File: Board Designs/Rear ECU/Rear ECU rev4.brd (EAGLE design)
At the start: 87.8 x 143.2 mm, 97 parts, among them X1 CONNECTOR-2, X2 CONNECTOR-6, X3 CONNECTOR-10MX150L_VERTICAL-10, X4 CONNECTOR-10MX150L_VERTICAL-10

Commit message: Rear ECU rev4: remove reference to unconnected/unused GPIO_CTRL3
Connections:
- removed net GPIO_CTRL3: U$3.D13
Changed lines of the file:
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@@
 <wire x1="22.987" y1="46.609" x2="21.463" y2="45.085" width="0.4064" layer="16"/>
-</signal>
-<signal name="GPIO_CTRL3">
-<contactref element="U$3" pad="D13"/>
 </signal>
 <signal name="GPIO_CTRL1">

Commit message: Add 15-pin .1" header to library, update copper rubout instructions on Enerdel board, add cooling control mosfet part numbers to Rear ECU schematic, fix silkscreen fuse names in Front ECU rev6
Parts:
- U$2, U$4, U$5: value N-CHANNEL_MOSFETGENERIC -> TK8R2A06PL
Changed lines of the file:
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@@
 <element name="C3" library="HyTechDevices" package="0805" value="1uF" x="78.701" y="114.366" rot="R90"/>
 <element name="C4" library="HyTechDevices" package="0805" value="1uF" x="72.758" y="109.894"/>
-<element name="U$2" library="HyTechDevices" package="TO-220-SINK" value="N-CHANNEL_MOSFETGENERIC" x="74.758" y="42.792">
+<element name="U$2" library="HyTechDevices" package="TO-220-SINK" value="TK8R2A06PL" x="74.758" y="42.792">
 <attribute name="_EXTERNAL_" value="1" x="74.758" y="42.792" size="1.778" layer="27" display="off"/>
 </element>
-<element name="U$4" library="HyTechDevices" package="TO-220-SINK" value="N-CHANNEL_MOSFETGENERIC" x="74.758" y="27.094">
+<element name="U$4" library="HyTechDevices" package="TO-220-SINK" value="TK8R2A06PL" x="74.758" y="27.094">
 <attribute name="_EXTERNAL_" value="1" x="74.758" y="27.094" size="1.778" layer="27" display="off"/>
 </element>
-<element name="U$5" library="HyTechDevices" package="TO-220-SINK" value="N-CHANNEL_MOSFETGENERIC" x="74.758" y="10.126">
+<element name="U$5" library="HyTechDevices" package="TO-220-SINK" value="TK8R2A06PL" x="74.758" y="10.126">
 <attribute name="_EXTERNAL_" value="1" x="74.758" y="10.126" size="1.778" layer="27" display="off"/>
 </element>

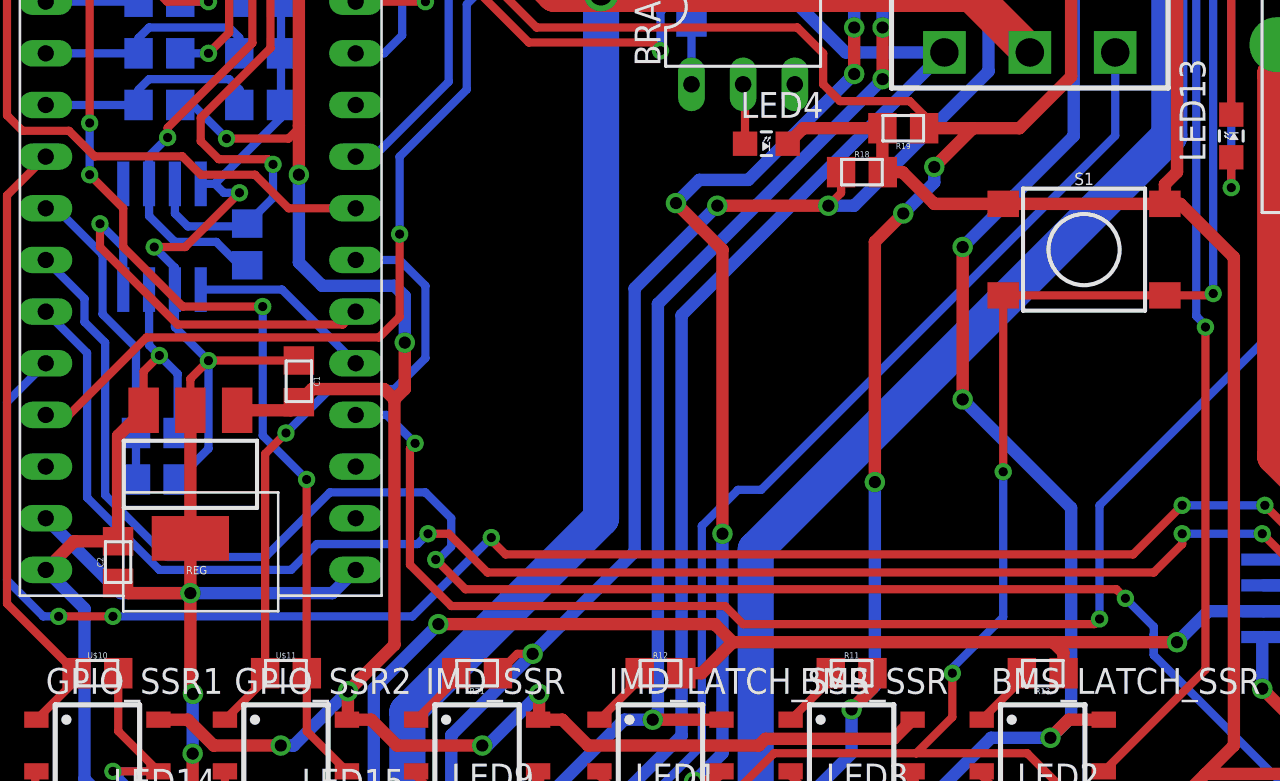
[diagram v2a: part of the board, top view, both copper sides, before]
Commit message: Added pulldown resistors to all gate drivers
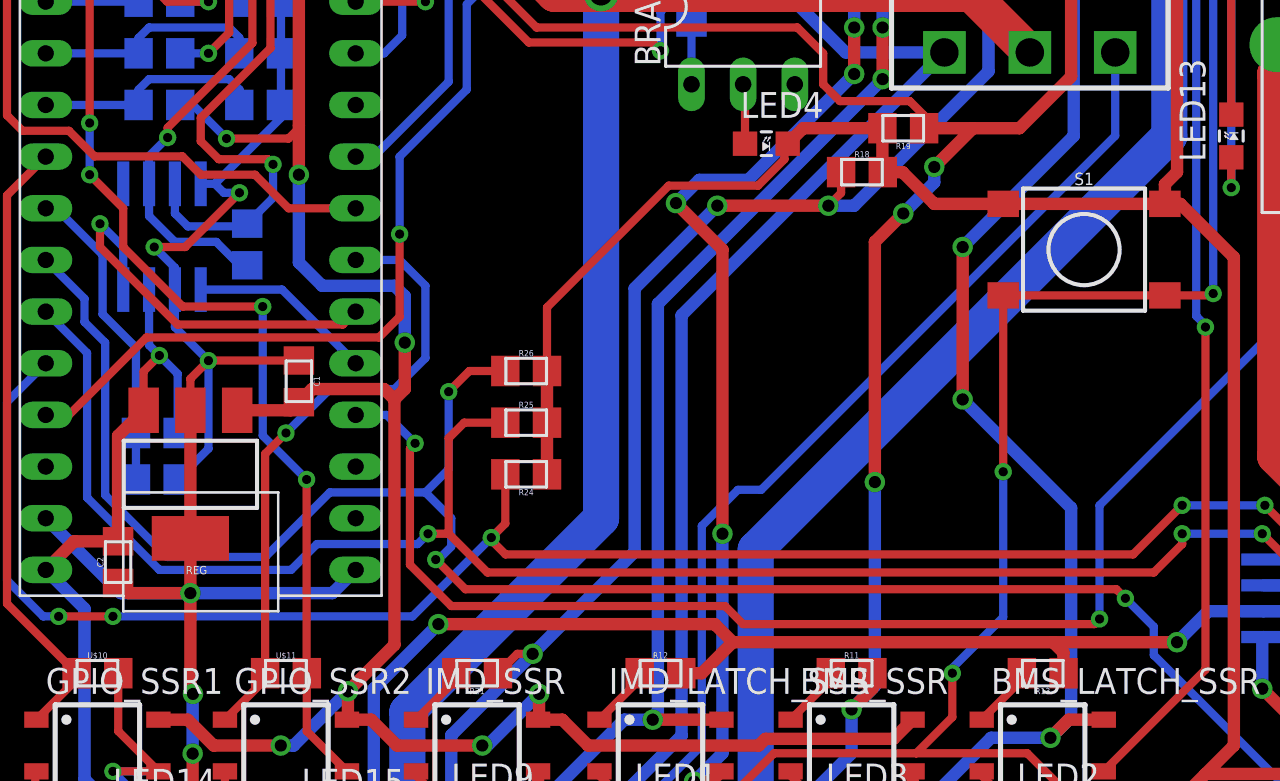
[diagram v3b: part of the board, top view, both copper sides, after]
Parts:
- added R24, R25, R26: 33, HyTechDevices:0805
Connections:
- net GND: now also R24.1, R25.2, R26.2
- net PWM_CTRL1: now also R24.2
- net PWM_CTRL2: now also R25.1
- net PWM_CTRL3: now also R26.1
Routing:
- net GND: track 522.5 -> 551.3 mm
- net PWM_CTRL2: track 80.3 -> 88.1 mm
- net PWM_CTRL3: track 102.9 -> 110.5 mm, vias 4 -> 5
- net PWM_CTRL1: track 85.2 -> 88.6 mm
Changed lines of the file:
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@@
 <?xml version="1.0" encoding="utf-8"?>
 <!DOCTYPE eagle SYSTEM "eagle.dtd">
-<eagle version="8.4.1">
+<eagle version="8.3.1">
 <drawing>
 <settings>
@@
 <param name="dpMaxLengthDifference" value="10mm"/>
 <param name="dpGapFactor" value="2.5"/>
+<param name="checkGrid" value="0"/>
 <param name="checkAngle" value="0"/>
 <param name="checkFont" value="1"/>
 <param name="checkRestrict" value="1"/>
-<param name="checkStop" value="0"/>
 <param name="useDiameter" value="13"/>
 <param name="maxErrors" value="50"/>
@@
 <element name="FSAE_FUSE" library="HyTechDevices" package="MINI-BLADE_FUSE_HOLDER" value="8A" x="24.384" y="138.43" rot="R180"/>
 <element name="SHUTDWN_FUSE" library="HyTechDevices" package="MINI-BLADE_FUSE_HOLDER" value="5A" x="7.112" y="78.232" rot="R90"/>
+<element name="R24" library="HyTechDevices" package="0805" value="33" x="27.94" y="40.894" rot="R180"/>
+<element name="R25" library="HyTechDevices" package="0805" value="33" x="27.94" y="43.434"/>
+<element name="R26" library="HyTechDevices" package="0805" value="33" x="27.94" y="45.974"/>
 </elements>
 <signals>
@@
 <wire x1="10.804" y1="40.64" x2="12.319" y2="42.155" width="0.4064" layer="16"/>
 <wire x1="12.319" y1="42.155" x2="12.319" y2="46.482" width="0.4064" layer="16"/>
-<wire x1="11.43" y1="44.044" x2="11.43" y2="37.744" width="0.6096" layer="1"/>
+<wire x1="11.43" y1="37.744" x2="11.43" y2="44.044" width="0.6096" layer="1"/>
 <via x="11.43" y="35.052" extent="1-16" drill="0.6"/>
-<wire x1="11.43" y1="37.744" x2="11.43" y2="35.052" width="0.6096" layer="1"/>
 <wire x1="7.874" y1="35.551" x2="8.373" y2="35.052" width="0.6096" layer="1"/>
-<wire x1="8.373" y1="35.052" x2="11.43" y2="35.052" width="0.6096" layer="1"/>
+<wire x1="11.43" y1="35.052" x2="8.373" y2="35.052" width="0.6096" layer="1"/>
 <wire x1="16.764" y1="104.405" x2="19.177" y2="106.818" width="0.6096" layer="16"/>
 <wire x1="19.177" y1="106.818" x2="19.177" y2="109.4994" width="0.6096" layer="16"/>
@@
 <wire x1="62.738" y1="51.562" x2="62.738" y2="27.559" width="0.6096" layer="1"/>
 <wire x1="62.738" y1="27.559" x2="61.341" y2="26.162" width="0.6096" layer="1"/>
-<wire x1="41.563" y1="57.912" x2="40.801" y2="57.15" width="0.6096" layer="1"/>
+<wire x1="40.801" y1="57.15" x2="41.563" y2="57.912" width="0.6096" layer="1"/>
 <wire x1="48.006" y1="54.193" x2="51.397" y2="54.193" width="0.6096" layer="1"/>
 <wire x1="19.558" y1="36.195" x2="18.415" y2="35.052" width="0.6096" layer="16"/>
@@
 <wire x1="33.81" y1="123.7528" x2="29.6912" y2="119.634" width="2.286" layer="16"/>
 <wire x1="29.6912" y1="119.634" x2="15.494" y2="119.634" width="2.286" layer="16"/>
+<contactref element="R24" pad="1"/>
+<contactref element="R25" pad="2"/>
+<contactref element="R26" pad="2"/>
+<wire x1="11.43" y1="37.744" x2="11.43" y2="35.052" width="0.6096" layer="1"/>
+<wire x1="28.965" y1="43.434" x2="28.965" y2="45.974" width="0.6096" layer="1"/>
+<wire x1="28.965" y1="43.434" x2="28.965" y2="40.894" width="0.6096" layer="1"/>
+<wire x1="28.965" y1="40.894" x2="28.965" y2="49.10253125" width="0.4064" layer="1"/>
+<wire x1="28.965" y1="49.10253125" x2="34.95026875" y2="55.0878" width="0.4064" layer="1"/>
+<wire x1="39.3398" y1="55.0878" x2="40.64" y2="56.388" width="0.4064" layer="1"/>
+<wire x1="34.95026875" y1="55.0878" x2="39.3398" y2="55.0878" width="0.4064" layer="1"/>
+<wire x1="40.64" y1="56.388" x2="40.64" y2="56.989" width="0.4064" layer="1"/>
+<wire x1="40.64" y1="56.989" x2="40.801" y2="57.15" width="0.4064" layer="1"/>
 </signal>
 <signal name="N$2">
@@
 <via x="57.404" y="34.798" extent="1-16" drill="0.45"/>
 <wire x1="57.404" y1="34.798" x2="58.801" y2="33.401" width="0.4064" layer="16"/>
-<wire x1="58.801" y1="33.02" x2="58.801" y2="33.401" width="0.4064" layer="16"/>
-<wire x1="58.801" y1="33.02" x2="58.801" y2="32.004" width="0.4064" layer="16"/>
 <wire x1="65.913" y1="24.892" x2="58.801" y2="32.004" width="0.4064" layer="16"/>
-<wire x1="58.801" y1="32.004" x2="58.801" y2="33.02" width="0.4064" layer="16"/>
+<wire x1="58.801" y1="32.004" x2="58.801" y2="33.401" width="0.4064" layer="16"/>
+<contactref element="R26" pad="1"/>
+<wire x1="26.915" y1="45.974" x2="25.146" y2="45.974" width="0.4064" layer="1"/>
+<wire x1="25.146" y1="45.974" x2="24.13" y2="44.958" width="0.4064" layer="1"/>
+<via x="24.13" y="44.958" extent="1-16" drill="0.45"/>
+<wire x1="24.13" y1="44.958" x2="24.13" y2="41.148" width="0.4064" layer="16"/>
+<wire x1="24.13" y1="41.148" x2="22.987" y2="40.005" width="0.4064" layer="16"/>
 </signal>
 <signal name="PWM_CTRL2">
@@
 <wire x1="22.606" y1="37.465" x2="17.653" y2="37.465" width="0.4064" layer="16"/>
 <wire x1="16.383" y1="36.195" x2="9.906" y2="36.195" width="0.4064" layer="16"/>
-<wire x1="23.114" y1="37.973" x2="24.13" y2="37.973" width="0.4064" layer="1"/>
+<wire x1="24.13" y1="37.973" x2="23.114" y2="37.973" width="0.4064" layer="1"/>
 <wire x1="24.13" y1="37.973" x2="26.035" y2="36.068" width="0.4064" layer="1"/>
 <wire x1="26.035" y1="36.068" x2="58.801" y2="36.068" width="0.4064" layer="1"/>
 <wire x1="58.801" y1="36.068" x2="60.198" y2="37.465" width="0.4064" layer="1"/>
 <wire x1="60.198" y1="37.465" x2="60.198" y2="37.973" width="0.4064" layer="1"/>
+<contactref element="R25" pad="1"/>
+<wire x1="26.915" y1="43.434" x2="24.892" y2="43.434" width="0.4064" layer="1"/>
+<wire x1="24.892" y1="43.434" x2="24.13" y2="42.672" width="0.4064" layer="1"/>
+<wire x1="24.13" y1="42.672" x2="24.13" y2="37.973" width="0.4064" layer="1"/>
 </signal>
 <signal name="PWM_CTRL1">
@@
 <wire x1="22.352" y1="33.909" x2="26.2255" y2="37.7825" width="0.4064" layer="16"/>
 <wire x1="60.198" y1="39.37" x2="57.785" y2="36.957" width="0.4064" layer="1"/>
-<wire x1="26.924" y1="36.957" x2="26.2255" y2="37.6555" width="0.4064" layer="1"/>
-<wire x1="26.2255" y1="37.6555" x2="26.2255" y2="37.7825" width="0.4064" layer="1"/>
+<wire x1="26.2255" y1="37.6555" x2="26.924" y2="36.957" width="0.4064" layer="1"/>
+<wire x1="26.2255" y1="37.7825" x2="26.2255" y2="37.6555" width="0.4064" layer="1"/>
 <via x="26.2255" y="37.7825" extent="1-16" drill="0.45"/>
 <wire x1="57.785" y1="36.957" x2="26.924" y2="36.957" width="0.4064" layer="1"/>
+<contactref element="R24" pad="2"/>
+<wire x1="26.915" y1="40.894" x2="26.915" y2="38.472" width="0.4064" layer="1"/>
+<wire x1="26.915" y1="38.472" x2="26.2255" y2="37.7825" width="0.4064" layer="1"/>
 </signal>
 <signal name="N$39">

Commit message: Finalize BSPD Test Board, FH Charger Control Board for manufacturing; Update silkscreen, schematic spacing on HV Board; Move updates from rev4 to rev5 of Rear ECU; add silkscreen, rotate thermistor connectors on BMS Segment board
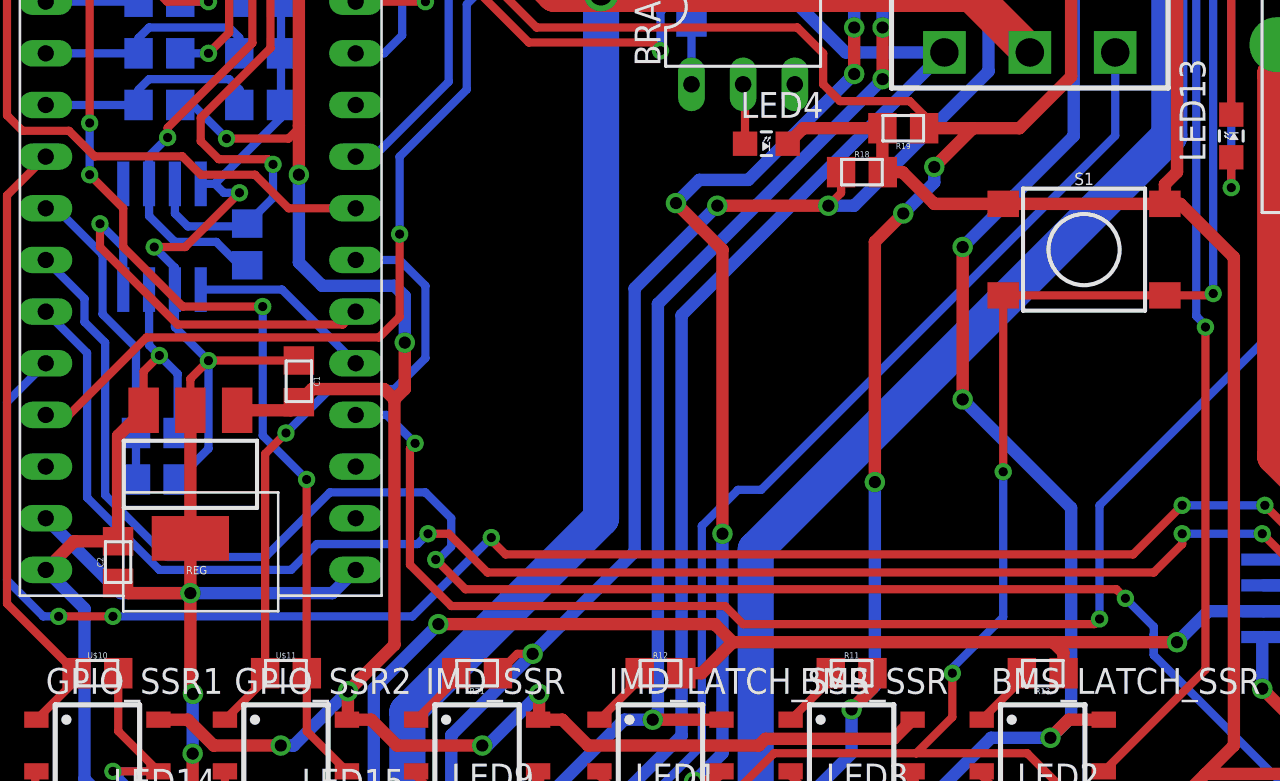
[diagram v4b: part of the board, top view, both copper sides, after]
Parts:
- removed R24, R25, R26: 33, HyTechDevices:0805
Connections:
- net GND: no longer R24.1, R25.2, R26.2
- net PWM_CTRL1: no longer R24.2
- net PWM_CTRL2: no longer R25.1
- net PWM_CTRL3: no longer R26.1
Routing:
- net GND: track 551.3 -> 522.5 mm
- net PWM_CTRL2: track 88.1 -> 80.3 mm
- net PWM_CTRL3: track 110.5 -> 102.9 mm, vias 5 -> 4
- net PWM_CTRL1: track 88.6 -> 85.2 mm
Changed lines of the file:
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@@
 <?xml version="1.0" encoding="utf-8"?>
 <!DOCTYPE eagle SYSTEM "eagle.dtd">
-<eagle version="8.3.1">
+<eagle version="8.4.1">
 <drawing>
 <settings>
@@
 <param name="dpMaxLengthDifference" value="10mm"/>
 <param name="dpGapFactor" value="2.5"/>
-<param name="checkGrid" value="0"/>
 <param name="checkAngle" value="0"/>
 <param name="checkFont" value="1"/>
 <param name="checkRestrict" value="1"/>
+<param name="checkStop" value="0"/>
 <param name="useDiameter" value="13"/>
 <param name="maxErrors" value="50"/>
@@
 <element name="FSAE_FUSE" library="HyTechDevices" package="MINI-BLADE_FUSE_HOLDER" value="8A" x="24.384" y="138.43" rot="R180"/>
 <element name="SHUTDWN_FUSE" library="HyTechDevices" package="MINI-BLADE_FUSE_HOLDER" value="5A" x="7.112" y="78.232" rot="R90"/>
-<element name="R24" library="HyTechDevices" package="0805" value="33" x="27.94" y="40.894" rot="R180"/>
-<element name="R25" library="HyTechDevices" package="0805" value="33" x="27.94" y="43.434"/>
-<element name="R26" library="HyTechDevices" package="0805" value="33" x="27.94" y="45.974"/>
 </elements>
 <signals>
@@
 <wire x1="10.804" y1="40.64" x2="12.319" y2="42.155" width="0.4064" layer="16"/>
 <wire x1="12.319" y1="42.155" x2="12.319" y2="46.482" width="0.4064" layer="16"/>
-<wire x1="11.43" y1="37.744" x2="11.43" y2="44.044" width="0.6096" layer="1"/>
+<wire x1="11.43" y1="44.044" x2="11.43" y2="37.744" width="0.6096" layer="1"/>
 <via x="11.43" y="35.052" extent="1-16" drill="0.6"/>
+<wire x1="11.43" y1="37.744" x2="11.43" y2="35.052" width="0.6096" layer="1"/>
 <wire x1="7.874" y1="35.551" x2="8.373" y2="35.052" width="0.6096" layer="1"/>
-<wire x1="11.43" y1="35.052" x2="8.373" y2="35.052" width="0.6096" layer="1"/>
+<wire x1="8.373" y1="35.052" x2="11.43" y2="35.052" width="0.6096" layer="1"/>
 <wire x1="16.764" y1="104.405" x2="19.177" y2="106.818" width="0.6096" layer="16"/>
 <wire x1="19.177" y1="106.818" x2="19.177" y2="109.4994" width="0.6096" layer="16"/>
@@
 <wire x1="62.738" y1="51.562" x2="62.738" y2="27.559" width="0.6096" layer="1"/>
 <wire x1="62.738" y1="27.559" x2="61.341" y2="26.162" width="0.6096" layer="1"/>
-<wire x1="40.801" y1="57.15" x2="41.563" y2="57.912" width="0.6096" layer="1"/>
+<wire x1="41.563" y1="57.912" x2="40.801" y2="57.15" width="0.6096" layer="1"/>
 <wire x1="48.006" y1="54.193" x2="51.397" y2="54.193" width="0.6096" layer="1"/>
 <wire x1="19.558" y1="36.195" x2="18.415" y2="35.052" width="0.6096" layer="16"/>
@@
 <wire x1="33.81" y1="123.7528" x2="29.6912" y2="119.634" width="2.286" layer="16"/>
 <wire x1="29.6912" y1="119.634" x2="15.494" y2="119.634" width="2.286" layer="16"/>
-<contactref element="R24" pad="1"/>
-<contactref element="R25" pad="2"/>
-<contactref element="R26" pad="2"/>
-<wire x1="11.43" y1="37.744" x2="11.43" y2="35.052" width="0.6096" layer="1"/>
-<wire x1="28.965" y1="43.434" x2="28.965" y2="45.974" width="0.6096" layer="1"/>
-<wire x1="28.965" y1="43.434" x2="28.965" y2="40.894" width="0.6096" layer="1"/>
-<wire x1="28.965" y1="40.894" x2="28.965" y2="49.10253125" width="0.4064" layer="1"/>
-<wire x1="28.965" y1="49.10253125" x2="34.95026875" y2="55.0878" width="0.4064" layer="1"/>
-<wire x1="39.3398" y1="55.0878" x2="40.64" y2="56.388" width="0.4064" layer="1"/>
-<wire x1="34.95026875" y1="55.0878" x2="39.3398" y2="55.0878" width="0.4064" layer="1"/>
-<wire x1="40.64" y1="56.388" x2="40.64" y2="56.989" width="0.4064" layer="1"/>
-<wire x1="40.64" y1="56.989" x2="40.801" y2="57.15" width="0.4064" layer="1"/>
 </signal>
 <signal name="N$2">
@@
 <via x="57.404" y="34.798" extent="1-16" drill="0.45"/>
 <wire x1="57.404" y1="34.798" x2="58.801" y2="33.401" width="0.4064" layer="16"/>
+<wire x1="58.801" y1="33.02" x2="58.801" y2="33.401" width="0.4064" layer="16"/>
+<wire x1="58.801" y1="33.02" x2="58.801" y2="32.004" width="0.4064" layer="16"/>
 <wire x1="65.913" y1="24.892" x2="58.801" y2="32.004" width="0.4064" layer="16"/>
-<wire x1="58.801" y1="32.004" x2="58.801" y2="33.401" width="0.4064" layer="16"/>
-<contactref element="R26" pad="1"/>
-<wire x1="26.915" y1="45.974" x2="25.146" y2="45.974" width="0.4064" layer="1"/>
-<wire x1="25.146" y1="45.974" x2="24.13" y2="44.958" width="0.4064" layer="1"/>
-<via x="24.13" y="44.958" extent="1-16" drill="0.45"/>
-<wire x1="24.13" y1="44.958" x2="24.13" y2="41.148" width="0.4064" layer="16"/>
-<wire x1="24.13" y1="41.148" x2="22.987" y2="40.005" width="0.4064" layer="16"/>
+<wire x1="58.801" y1="32.004" x2="58.801" y2="33.02" width="0.4064" layer="16"/>
 </signal>
 <signal name="PWM_CTRL2">
@@
 <wire x1="22.606" y1="37.465" x2="17.653" y2="37.465" width="0.4064" layer="16"/>
 <wire x1="16.383" y1="36.195" x2="9.906" y2="36.195" width="0.4064" layer="16"/>
-<wire x1="24.13" y1="37.973" x2="23.114" y2="37.973" width="0.4064" layer="1"/>
+<wire x1="23.114" y1="37.973" x2="24.13" y2="37.973" width="0.4064" layer="1"/>
 <wire x1="24.13" y1="37.973" x2="26.035" y2="36.068" width="0.4064" layer="1"/>
 <wire x1="26.035" y1="36.068" x2="58.801" y2="36.068" width="0.4064" layer="1"/>
 <wire x1="58.801" y1="36.068" x2="60.198" y2="37.465" width="0.4064" layer="1"/>
 <wire x1="60.198" y1="37.465" x2="60.198" y2="37.973" width="0.4064" layer="1"/>
-<contactref element="R25" pad="1"/>
-<wire x1="26.915" y1="43.434" x2="24.892" y2="43.434" width="0.4064" layer="1"/>
-<wire x1="24.892" y1="43.434" x2="24.13" y2="42.672" width="0.4064" layer="1"/>
-<wire x1="24.13" y1="42.672" x2="24.13" y2="37.973" width="0.4064" layer="1"/>
 </signal>
 <signal name="PWM_CTRL1">
@@
 <wire x1="22.352" y1="33.909" x2="26.2255" y2="37.7825" width="0.4064" layer="16"/>
 <wire x1="60.198" y1="39.37" x2="57.785" y2="36.957" width="0.4064" layer="1"/>
-<wire x1="26.2255" y1="37.6555" x2="26.924" y2="36.957" width="0.4064" layer="1"/>
-<wire x1="26.2255" y1="37.7825" x2="26.2255" y2="37.6555" width="0.4064" layer="1"/>
+<wire x1="26.924" y1="36.957" x2="26.2255" y2="37.6555" width="0.4064" layer="1"/>
+<wire x1="26.2255" y1="37.6555" x2="26.2255" y2="37.7825" width="0.4064" layer="1"/>
 <via x="26.2255" y="37.7825" extent="1-16" drill="0.45"/>
 <wire x1="57.785" y1="36.957" x2="26.924" y2="36.957" width="0.4064" layer="1"/>
-<contactref element="R24" pad="2"/>
-<wire x1="26.915" y1="40.894" x2="26.915" y2="38.472" width="0.4064" layer="1"/>
-<wire x1="26.915" y1="38.472" x2="26.2255" y2="37.7825" width="0.4064" layer="1"/>
 </signal>
 <signal name="N$39">
